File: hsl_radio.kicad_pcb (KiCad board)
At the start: 4 copper layers, 95.9 x 90.2 mm, 71 parts, among them J2 CC Prog/Debug, J4 UART1, J5 Control Outputs, J6 ANT, U1 AP62300TWU-7, U2 CC1110, U3 SF2446E, U5 TLV803S, U6 PE4259, U7 0433BM15A0001, U8 FT5HN 27MHz

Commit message: Preparing for JLCPCB
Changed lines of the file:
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@@
     (grid_origin 113.5 88.5)
     (pcbplotparams
-      (layerselection 0x00010fc_80000007)
-      (plot_on_all_layers_selection 0x0000000_00000000)
+      (layerselection 0x00010fc_ffffffff)
+      (plot_on_all_layers_selection 0x00010fc_80000007)
       (disableapertmacros false)
       (usegerberextensions true)
@@
     (fp_line (start 1.6 0.8) (end -1.6 0.8)
       (stroke (width 0.1) (type solid)) (layer "F.Fab"))
-    (pad "1" smd roundrect (at -1.575 0 180) (size 1.05 1.9) (layers "F.Cu" "F.Paste" "F.Mask") (roundrect_rratio 0.238095)
+    (pad "1" smd roundrect (at -1.575 0 180) (size 1.05 1.9) (layers "F.Cu" "F.Paste" "F.Mask") (roundrect_rratio 0.2380952381)
       (net 3 "+3V3") (pintype "passive"))
-    (pad "2" smd roundrect (at 1.575 0 180) (size 1.05 1.9) (layers "F.Cu" "F.Paste" "F.Mask") (roundrect_rratio 0.238095)
+    (pad "2" smd roundrect (at 1.575 0 180) (size 1.05 1.9) (layers "F.Cu" "F.Paste" "F.Mask") (roundrect_rratio 0.2380952381)
       (net 36 "Net-(U4-Pin_57)") (pintype "passive"))
     (model "${KICAD6_3DMODEL_DIR}/Inductor_SMD.3dshapes/L_1206_3216Metric.wrl"
@@
     (fp_line (start 1.6 0.8) (end -1.6 0.8)
       (stroke (width 0.1) (type solid)) (layer "F.Fab"))
-    (pad "1" smd roundrect (at -1.575 0 180) (size 1.05 1.9) (layers "F.Cu" "F.Paste" "F.Mask") (roundrect_rratio 0.238095)
+    (pad "1" smd roundrect (at -1.575 0 180) (size 1.05 1.9) (layers "F.Cu" "F.Paste" "F.Mask") (roundrect_rratio 0.2380952381)
       (net 17 "Net-(U1-EN)") (pintype "passive"))
-    (pad "2" smd roundrect (at 1.575 0 180) (size 1.05 1.9) (layers "F.Cu" "F.Paste" "F.Mask") (roundrect_rratio 0.238095)
+    (pad "2" smd roundrect (at 1.575 0 180) (size 1.05 1.9) (layers "F.Cu" "F.Paste" "F.Mask") (roundrect_rratio 0.2380952381)
       (net 93 "+BATT") (pintype "passive"))
     (model "${KICAD6_3DMODEL_DIR}/Inductor_SMD.3dshapes/L_1206_3216Metric.wrl"

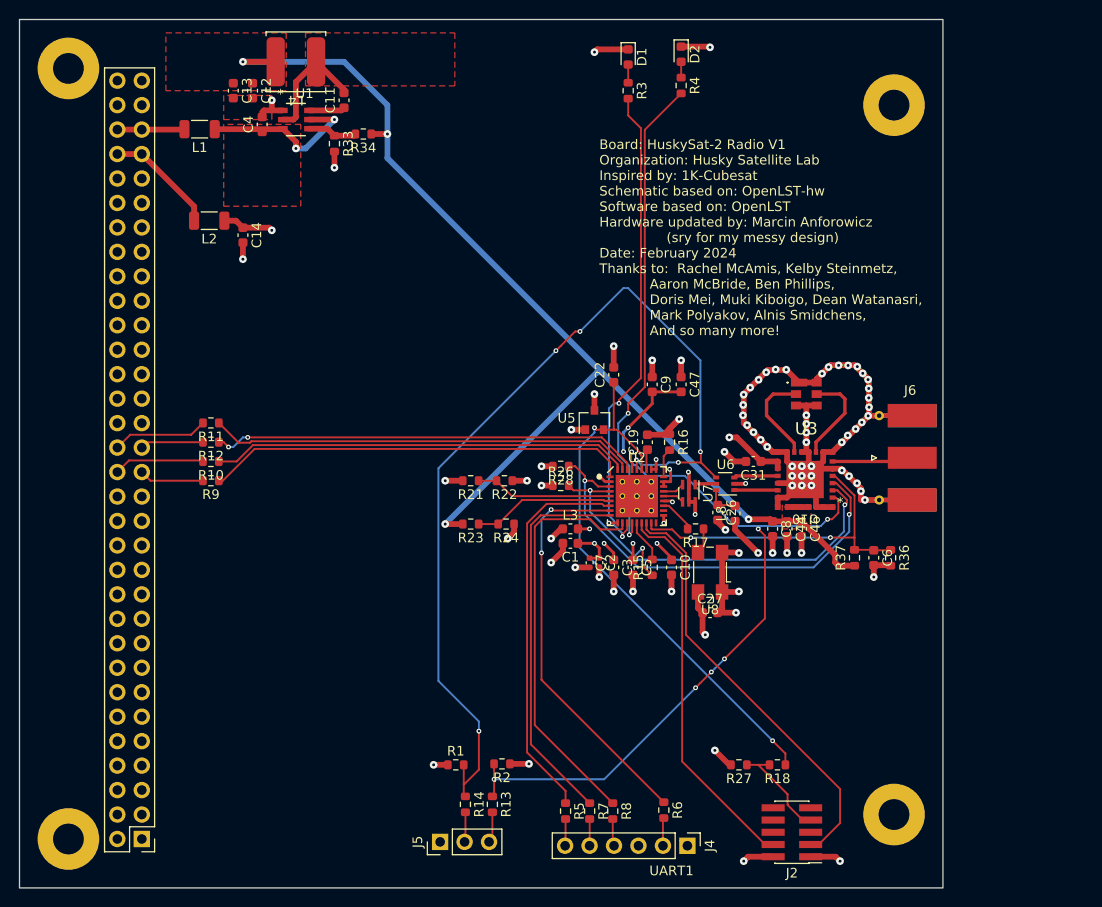
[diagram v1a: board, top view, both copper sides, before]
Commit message: Added test points
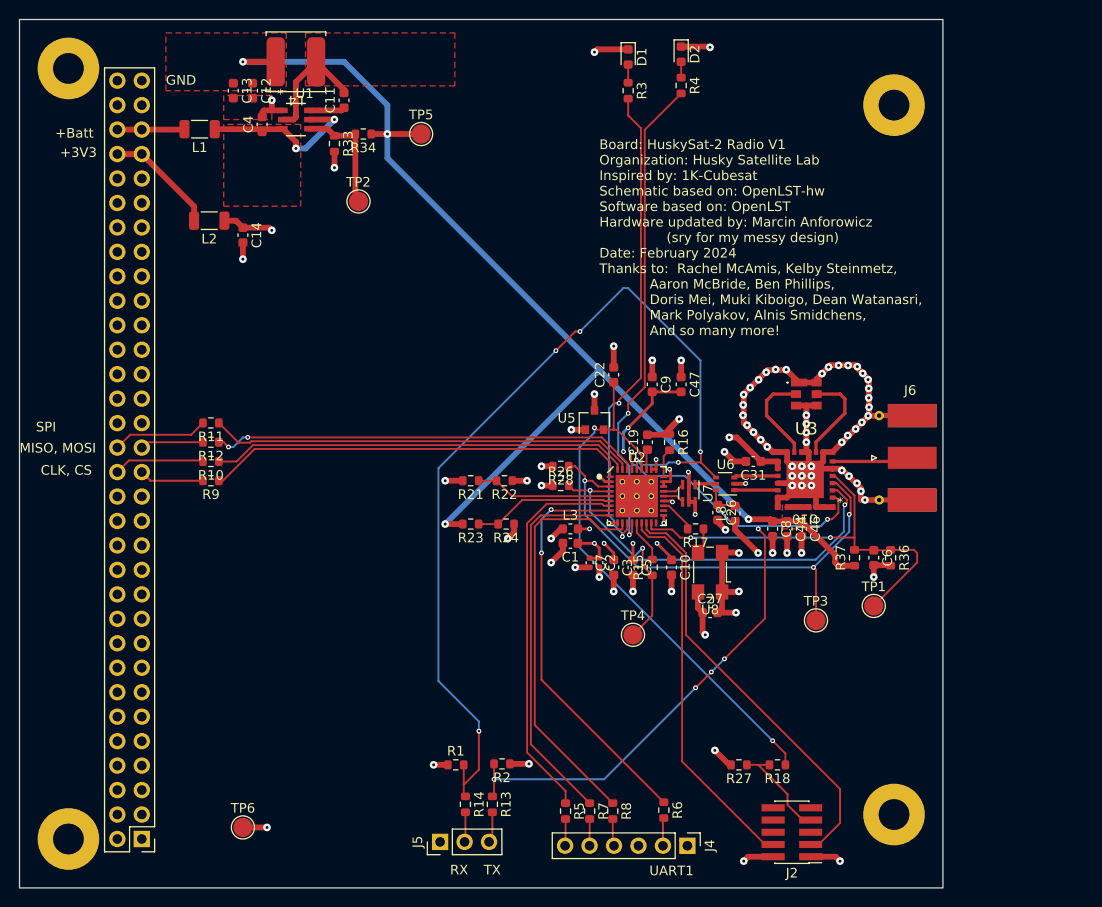
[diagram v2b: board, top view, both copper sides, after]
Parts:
- added TP1: PA_VAPC, TestPoint:TestPoint_Pad_D2.0mm, F.Cu at (167.5, 78.0)
- added TP2: FB, TestPoint:TestPoint_Pad_D2.0mm, F.Cu at (114.0, 36.0)
- added TP3: RF_BYP, TestPoint:TestPoint_Pad_D2.0mm, F.Cu at (161.5, 79.5)
- added TP4: RF_EN, TestPoint:TestPoint_Pad_D2.0mm, F.Cu at (142.5, 81.0)
- added TP5: 3V9, TestPoint:TestPoint_Pad_D2.0mm, F.Cu at (120.5, 29.0)
- added TP6: GND, TestPoint:TestPoint_Pad_D2.0mm, F.Cu at (102.0, 101.0)
- U10: value ~ -> SKY65366-21
- U4: value ~ -> PCI-104
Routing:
- net /PA_VAPC: track 34.7 -> 44.9 mm
- net Net-(U1-FB): track 5.20 -> 12.3 mm
- net /RF_EN: track 46.1 -> 53.1 mm
- net /RF_BYP: track 46.3 -> 51.9 mm, vias 2 -> 3
- net +3V9: track 121.1 -> 124.6 mm
- net GND: track 154.0 -> 156.5 mm, vias 78 -> 79
